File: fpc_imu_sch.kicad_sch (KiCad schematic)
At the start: 7 parts, among them U4 ASM330LHHXTR

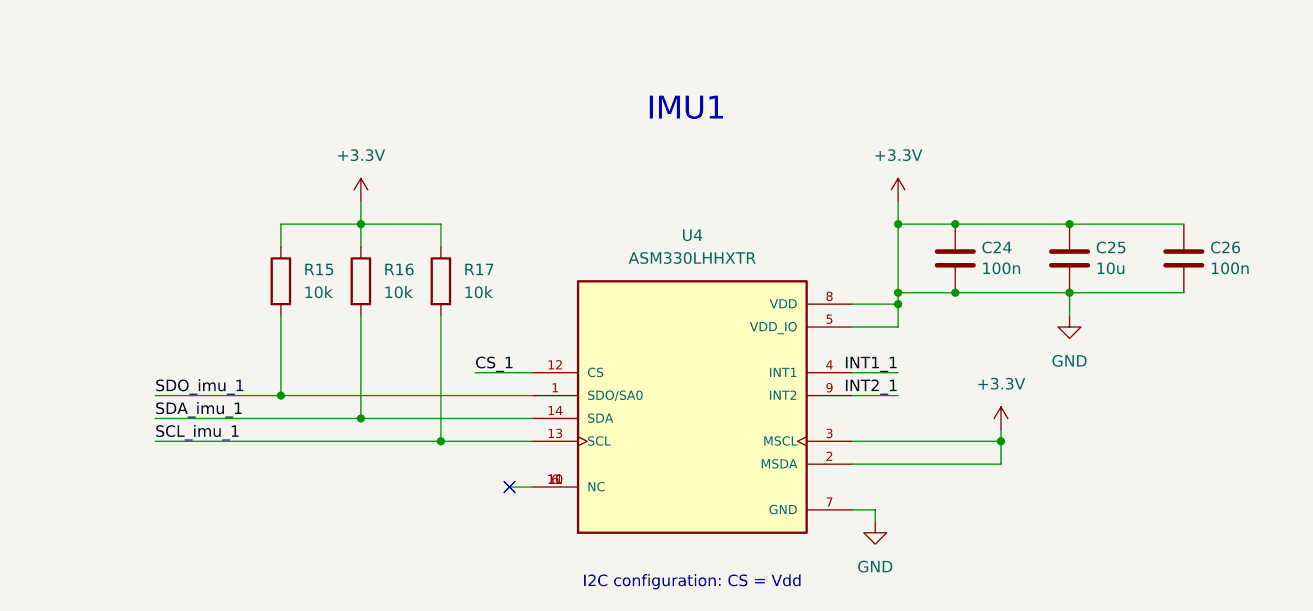
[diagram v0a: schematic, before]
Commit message: discarded 24MHz crystal. ERC passed 1st time
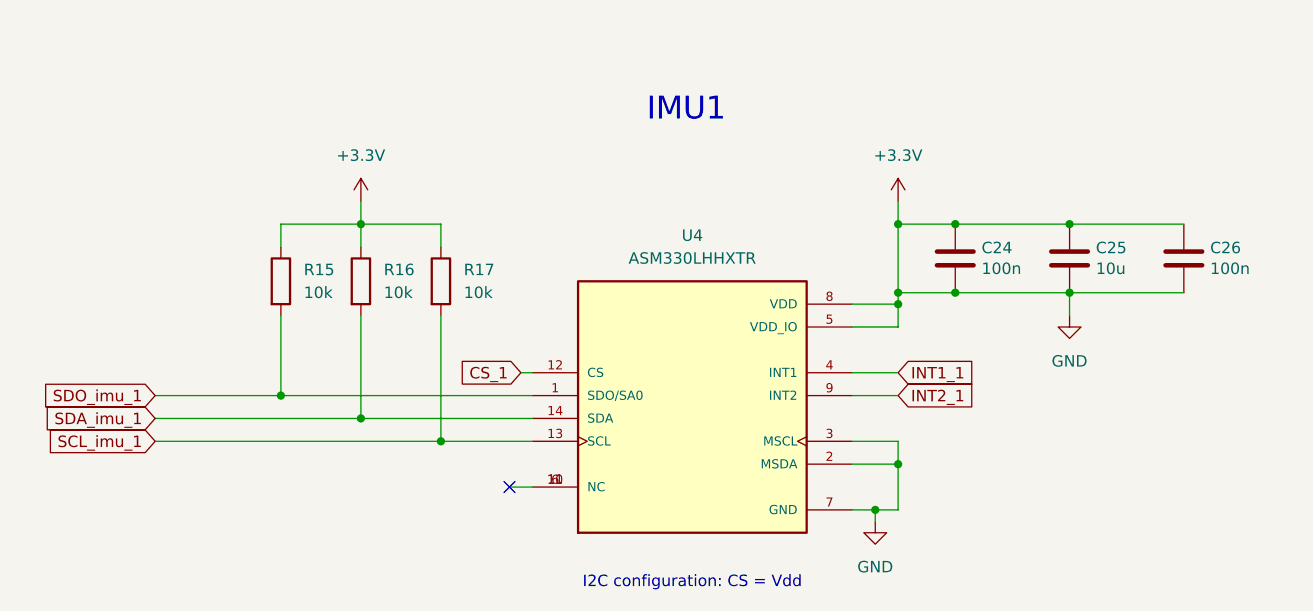
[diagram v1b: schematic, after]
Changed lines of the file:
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@@
+	)
+	(junction
+		(at 111.76 81.28)
+		(diameter 0)
+		(color 0 0 0 0)
 	)
 	(junction
@@
 	)
 	(junction
-		(at 125.73 73.66)
-		(diameter 0)
-		(color 0 0 0 0)
-	)
-	(junction
 		(at 45.72 68.58)
+		(diameter 0)
+		(color 0 0 0 0)
+	)
+	(junction
+		(at 114.3 76.2)
 		(diameter 0)
 		(color 0 0 0 0)
@@
 	(wire
 		(pts
-			(xy 125.73 73.66) (xy 125.73 72.39)
+			(xy 114.3 81.28) (xy 111.76 81.28)
 		)
 		(stroke
@@
 	(wire
 		(pts
-			(xy 67.31 66.04) (xy 73.66 66.04)
+			(xy 72.39 66.04) (xy 73.66 66.04)
 		)
 		(stroke
@@
 	(wire
 		(pts
-			(xy 125.73 76.2) (xy 125.73 73.66)
-		)
-		(stroke
-			(width 0)
-			(type default)
-		)
-	)
-	(wire
-		(pts
 			(xy 31.75 71.12) (xy 54.61 71.12)
 		)
@@
 	(wire
 		(pts
-			(xy 109.22 73.66) (xy 125.73 73.66)
-		)
-		(stroke
-			(width 0)
-			(type default)
-		)
-	)
-	(wire
-		(pts
-			(xy 109.22 76.2) (xy 125.73 76.2)
+			(xy 109.22 73.66) (xy 114.3 73.66)
+		)
+		(stroke
+			(width 0)
+			(type default)
+		)
+	)
+	(wire
+		(pts
+			(xy 109.22 76.2) (xy 114.3 76.2)
 		)
 		(stroke
@@
 	(wire
 		(pts
+			(xy 114.3 73.66) (xy 114.3 76.2)
+		)
+		(stroke
+			(width 0)
+			(type default)
+		)
+	)
+	(wire
+		(pts
 			(xy 114.3 49.53) (xy 114.3 46.99)
 		)
@@
 	(wire
 		(pts
+			(xy 114.3 76.2) (xy 114.3 81.28)
+		)
+		(stroke
+			(width 0)
+			(type default)
+		)
+	)
+	(wire
+		(pts
 			(xy 109.22 58.42) (xy 114.3 58.42)
 		)
@@
 		)
 	)
-	(label "CS_1"
-		(at 67.31 66.04 0)
+	(global_label "SDO_imu_1"
+		(shape input)
+		(at 31.75 68.58 180)
+		(fields_autoplaced yes)
 		(effects
 			(font
 				(size 1.27 1.27)
 			)
-			(justify left bottom)
-		)
-	)
-	(label "SDA_imu_1"
-		(at 31.75 71.12 0)
+			(justify right)
+		)
+		(property "Intersheetrefs" "${INTERSHEET_REFS}"
+			(at 18.363 68.58 0)
+			(effects
+				(font
+					(size 1.27 1.27)
+				)
+				(justify right)
+				(hide yes)
+			)
+		)
+	)
+	(global_label "INT2_1"
+		(shape input)
+		(at 114.3 68.58 0)
+		(fields_autoplaced yes)
 		(effects
 			(font
 				(size 1.27 1.27)
 			)
-			(justify left bottom)
-		)
-	)
-	(label "SDO_imu_1"
-		(at 31.75 68.58 0)
+			(justify left)
+		)
+		(property "Intersheetrefs" "${INTERSHEET_REFS}"
+			(at 123.5747 68.58 0)
+			(effects
+				(font
+					(size 1.27 1.27)
+				)
+				(justify left)
+				(hide yes)
+			)
+		)
+	)
+	(global_label "INT1_1"
+		(shape input)
+		(at 114.3 66.04 0)
+		(fields_autoplaced yes)
 		(effects
 			(font
 				(size 1.27 1.27)
 			)
-			(justify left bottom)
-		)
-	)
-	(label "INT1_1"
-		(at 114.3 66.04 180)
+			(justify left)
+		)
+		(property "Intersheetrefs" "${INTERSHEET_REFS}"
+			(at 123.5747 66.04 0)
+			(effects
+				(font
+					(size 1.27 1.27)
+				)
+				(justify left)
+				(hide yes)
+			)
+		)
+	)
+	(global_label "SCL_imu_1"
+		(shape input)
+		(at 31.75 73.66 180)
+		(fields_autoplaced yes)
 		(effects
 			(font
 				(size 1.27 1.27)
 			)
-			(justify right bottom)
-		)
-	)
-	(label "SCL_imu_1"
-		(at 31.75 73.66 0)
+			(justify right)
+		)
+		(property "Intersheetrefs" "${INTERSHEET_REFS}"
+			(at 18.6654 73.66 0)
+			(effects
+				(font
+					(size 1.27 1.27)
+				)
+				(justify right)
+				(hide yes)
+			)
+		)
+	)
+	(global_label "SDA_imu_1"
+		(shape input)
+		(at 31.75 71.12 180)
+		(fields_autoplaced yes)
 		(effects
 			(font
 				(size 1.27 1.27)
 			)
-			(justify left bottom)
-		)
-	)
-	(label "INT2_1"
-		(at 114.3 68.58 180)
+			(justify right)
+		)
+		(property "Intersheetrefs" "${INTERSHEET_REFS}"
+			(at 18.6049 71.12 0)
+			(effects
+				(font
+					(size 1.27 1.27)
+				)
+				(justify right)
+				(hide yes)
+			)
+		)
+	)
+	(global_label "CS_1"
+		(shape input)
+		(at 72.39 66.04 180)
+		(fields_autoplaced yes)
 		(effects
 			(font
 				(size 1.27 1.27)
 			)
-			(justify right bottom)
+			(justify right)
+		)
+		(property "Intersheetrefs" "${INTERSHEET_REFS}"
+			(at 64.7482 66.04 0)
+			(effects
+				(font
+					(size 1.27 1.27)
+				)
+				(justify right)
+				(hide yes)
+			)
 		)
 	)
@@
 					(unit 1)
 				)
-			)
-		)
-	)
-	(symbol
-		(lib_id "power:+3.3V")
-		(at 125.73 72.39 0)
-		(unit 1)
-		(exclude_from_sim no)
-		(in_bom yes)
-		(on_board yes)
-		(dnp no)
-		(fields_autoplaced yes)
-		(property "Reference" "#PWR050"
-			(at 125.73 76.2 0)
-			(effects
-				(font
-					(size 1.27 1.27)
-				)
-				(hide yes)
-			)
-		)
-		(property "Value" "+3.3V"
-			(at 125.73 67.31 0)
-			(effects
-				(font
-					(size 1.27 1.27)
-				)
-			)
-		)
-		(property "Footprint" ""
-			(at 125.73 72.39 0)
-			(effects
-				(font
-					(size 1.27 1.27)
-				)
-				(hide yes)
-			)
-		)
-		(property "Datasheet" ""
-			(at 125.73 72.39 0)
-			(effects
-				(font
-					(size 1.27 1.27)
-				)
-				(hide yes)
-			)
-		)
-		(property "Description" "Power symbol creates a global label with name \"+3.3V\""
-			(at 125.73 72.39 0)
-			(effects
-				(font
-					(size 1.27 1.27)
-				)
-				(hide yes)
-			)
-		)
-		(pin "1"
-		)
-		(instances
-			(project "FPSP Camera"
-				(path "/b8279e3f-7ea4-46f5-abf2-a9173e16562f/fe27d215-4a03-48dc-b9d9-ef5c7fd8f22c"
-					(reference "#PWR050")
-					(unit 1)
-				)

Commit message: updates in layout
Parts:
- removed U4: ASM330LHHXTR, ASM330LHHXTR:XDCR_ASM330LHHXTR, symbol ASM330LHHXTR:ASM330LHHXTR
- added U3: ASM330LHHXTR, ASM330LHHXTR:XDCR_ASM330LHHXTR, symbol ASM330LHHXTR:ASM330LHHXTR
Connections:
- net +3.3V: now also U3.2 (MSDA), U3.3 (MSCL), U3.5 (VDD_IO), U3.8 (VDD); no longer C24.2, C25.2, C26.2
- net CS_1: now also U3.12 (CS)
- net INT1_1: now also U3.4 (INT1)
- net INT2_1: now also U3.9 (INT2)
- net SCL_imu_1: now also U3.13 (SCL)
- net SDA_imu_1: now also U3.14 (SDA)
- net SDO_imu_1: now also U3.1 (SDO/SA0)
- new net: U3.10 (NC), U3.11 (NC), U3.6 (NC)
- new net GND: C24.2, C25.2, C26.2, U3.7 (GND)
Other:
- moved on the sheet: C24, C25, C26
